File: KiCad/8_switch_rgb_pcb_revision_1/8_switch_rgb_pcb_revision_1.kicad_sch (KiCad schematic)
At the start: 97 parts, among them SW0 SW0, SW1 SW1, SW2 SW2, SW3 SW3, SW4 SW4, SW5 SW5, SW6 SW6, SW7 SW7, U2 74HC165, Y1 16MHz

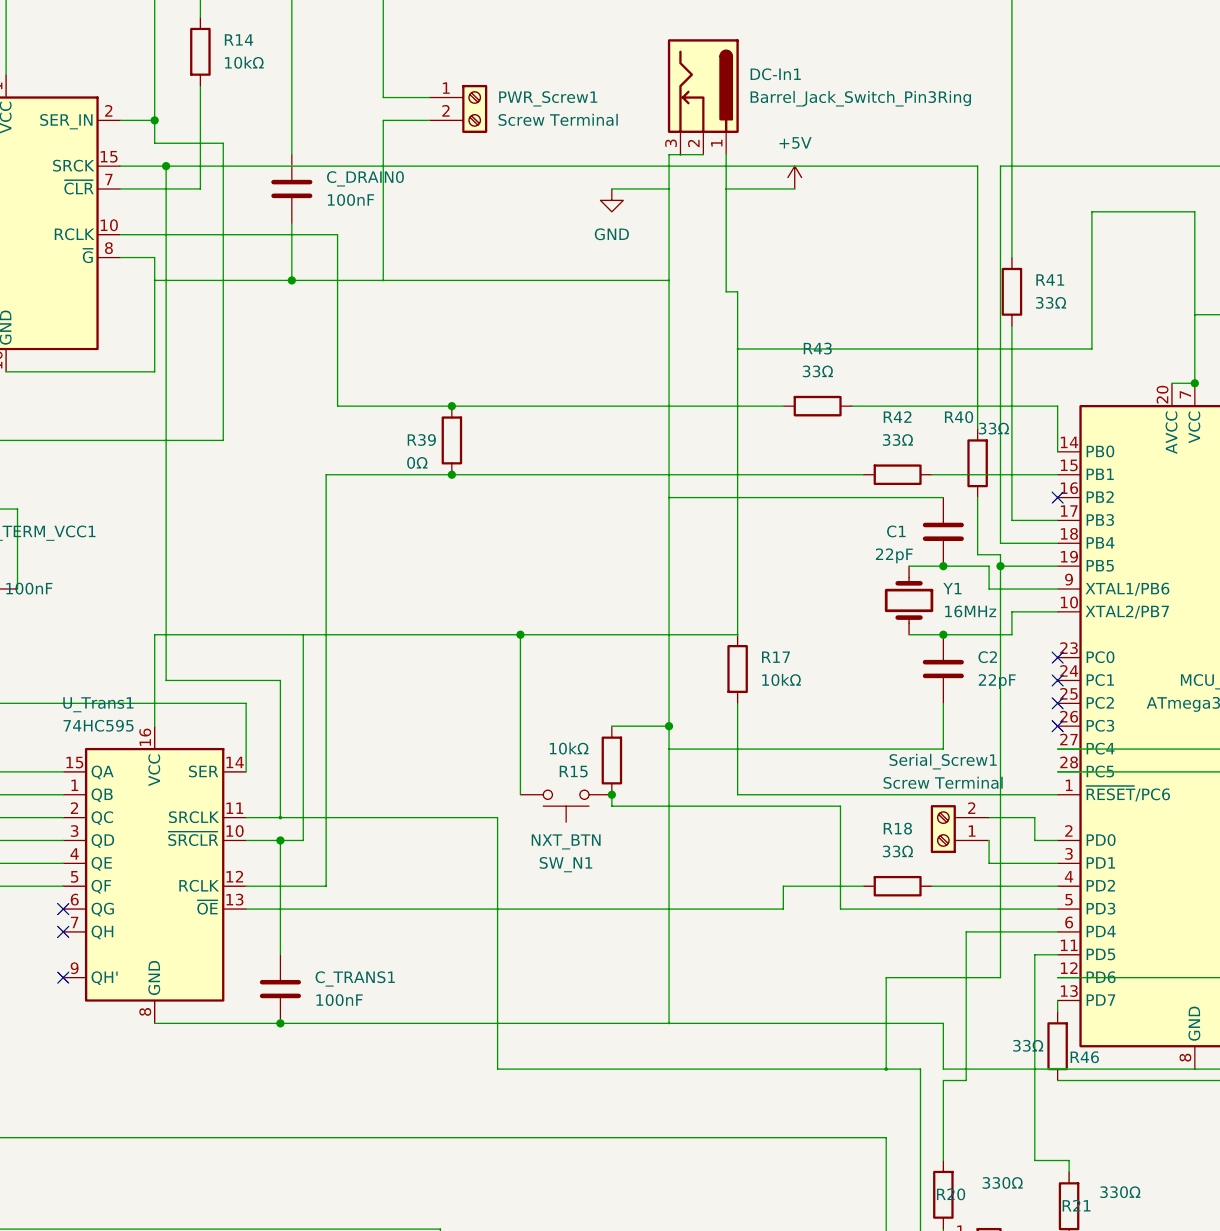
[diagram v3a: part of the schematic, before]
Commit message: Added gerbers, will look at ground plane
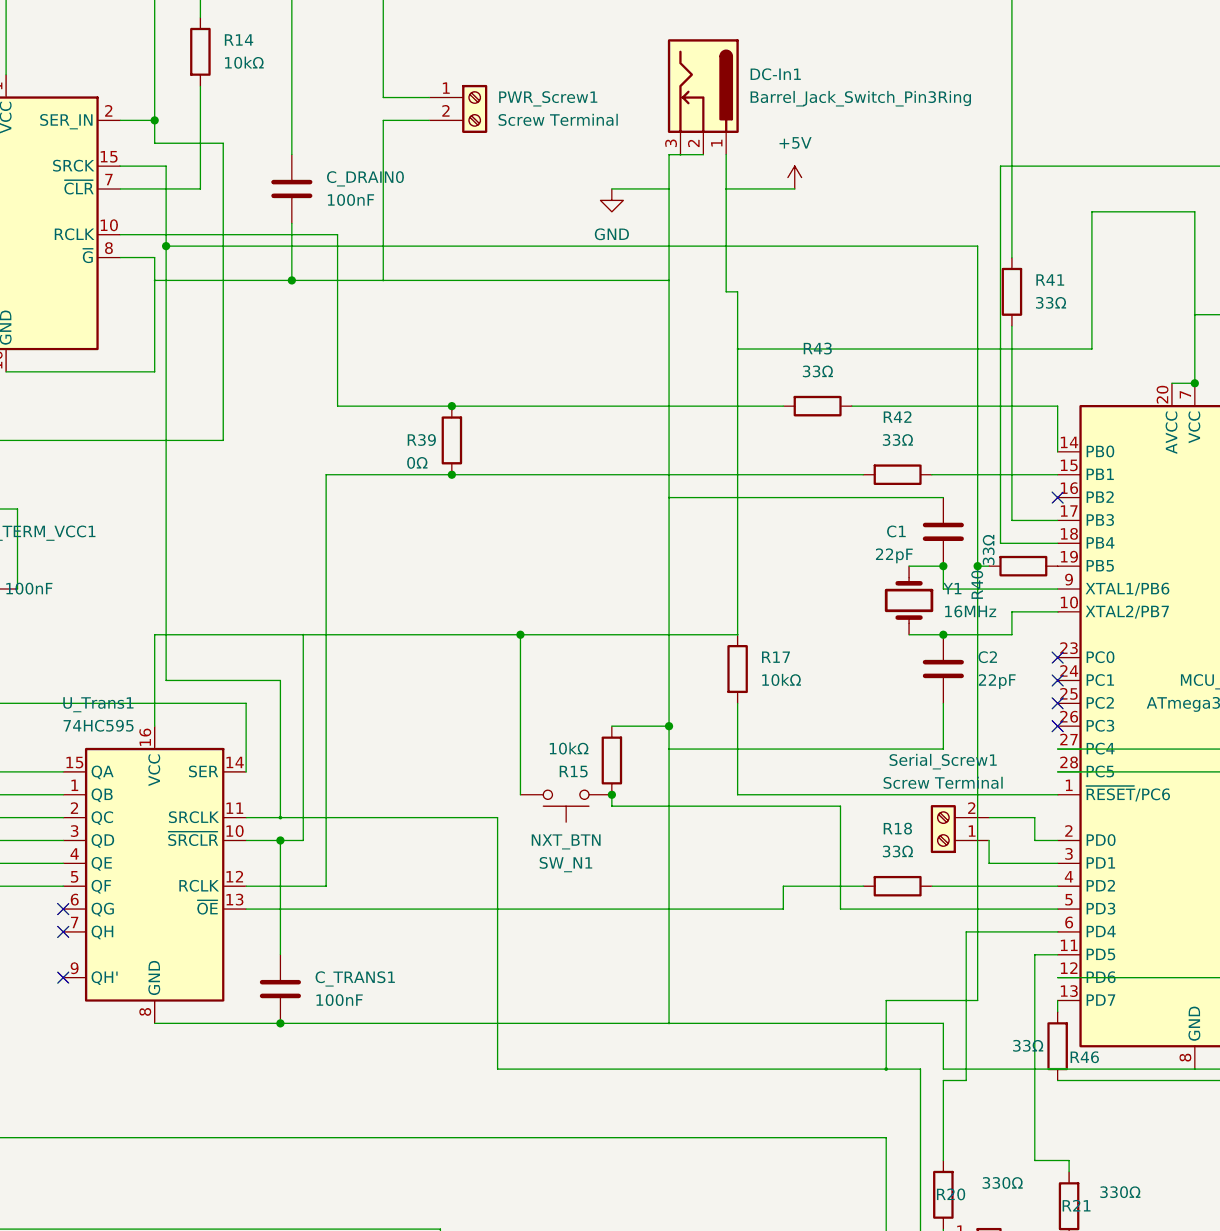
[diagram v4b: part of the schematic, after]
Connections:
- net at R22.1, R40.2, U2.2 (CP)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: no longer MCU_1.19 (PB5), R40.1
- new net: MCU_1.19 (PB5), R40.1
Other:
- moved on the sheet: R40
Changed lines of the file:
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@@
   (junction (at 113.03 83.82) (diameter 0) (color 0 0 0 0)
   )
-  (junction (at 238.76 81.28) (diameter 0) (color 0 0 0 0)
-  )
   (junction (at 177.8 63.5) (diameter 0) (color 0 0 0 0)
   )
@@
   (junction (at 326.39 41.91) (diameter 0) (color 0 0 0 0)
   )
+  (junction (at 146.05 45.72) (diameter 0) (color 0 0 0 0)
+  )
   (junction (at 201.93 39.37) (diameter 0.2) (color 0 0 0 1)
   )
@@
   (junction (at 114.3 180.34) (diameter 0) (color 0 0 0 0)
   )
+  (junction (at 236.22 81.28) (diameter 0) (color 0 0 0 0)
+  )
   (junction (at 304.8 82.55) (diameter 0) (color 0 0 0 0)
   )
@@
   (junction (at 392.43 111.76) (diameter 0.2) (color 255 0 0 1)
   )
-  (junction (at 146.05 36.83) (diameter 0) (color 0 0 0 0)
-  )
   (junction (at 69.85 119.38) (diameter 0) (color 0 0 0 0)
   )
@@
     (stroke (width 0) (type default))
   )
-  (wire (pts (xy 245.11 83.82) (xy 237.49 83.82))
+  (wire (pts (xy 232.41 83.82) (xy 245.11 83.82))
     (stroke (width 0) (type default))
   )
@@
     (stroke (width 0.2) (type default) (color 255 0 0 1))
   )
-  (wire (pts (xy 236.22 36.83) (xy 236.22 66.04))
-    (stroke (width 0.3) (type default) (color 255 255 0 1))
-  )
   (wire (pts (xy 92.71 34.29) (xy 72.39 34.29))
     (stroke (width 0) (type default))
@@
     (stroke (width 0.2) (type default) (color 255 0 0 1))
   )
-  (wire (pts (xy 236.22 73.66) (xy 236.22 80.01))
-    (stroke (width 0.3) (type default) (color 255 255 0 1))
-  )
   (wire (pts (xy 115.57 49.53) (xy 113.03 49.53))
     (stroke (width 0) (type default))
@@
     (stroke (width 0) (type default))
   )
-  (wire (pts (xy 238.76 81.28) (xy 238.76 127))
-    (stroke (width 0.3) (type default) (color 255 255 0 1))
-  )
   (wire (pts (xy 67.31 170.18) (xy 63.5 170.18))
     (stroke (width 0) (type default))
@@
     (stroke (width 0) (type default))
   )
-  (wire (pts (xy 238.76 81.28) (xy 245.11 81.28))
-    (stroke (width 0.3) (type default) (color 255 255 0 1))
-  )
   (wire (pts (xy 60.96 217.17) (xy 60.96 208.28))
     (stroke (width 0) (type default))
@@
     (stroke (width 0) (type default))
   )
+  (wire (pts (xy 146.05 36.83) (xy 146.05 45.72))
+    (stroke (width 0.3) (type default) (color 255 255 0 1))
+  )
   (wire (pts (xy 115.57 34.29) (xy 100.33 34.29))
     (stroke (width 0) (type default))
@@
     (stroke (width 0) (type default))
   )
-  (wire (pts (xy 226.06 137.16) (xy 226.06 127))
+  (wire (pts (xy 226.06 137.16) (xy 226.06 129.54))
     (stroke (width 0.3) (type default) (color 255 255 0 1))
   )
@@
     (stroke (width 0) (type default))
   )
-  (wire (pts (xy 146.05 36.83) (xy 236.22 36.83))
-    (stroke (width 0.3) (type default) (color 255 255 0 1))
-  )
   (wire (pts (xy 360.68 168.91) (xy 360.68 138.43))
     (stroke (width 0) (type default))
@@
     (stroke (width 0.3) (type default) (color 255 255 0 1))
   )
-  (wire (pts (xy 237.49 83.82) (xy 237.49 81.28))
-    (stroke (width 0) (type default))
-  )
   (wire (pts (xy 365.76 167.64) (xy 398.78 167.64))
     (stroke (width 0.2) (type default) (color 0 0 0 1))
@@
     (stroke (width 0) (type default))
   )
-  (wire (pts (xy 226.06 127) (xy 238.76 127))
+  (wire (pts (xy 226.06 129.54) (xy 236.22 129.54))
     (stroke (width 0.3) (type default) (color 255 255 0 1))
   )
@@
     (stroke (width 0.2) (type default) (color 255 0 0 1))
   )
+  (wire (pts (xy 146.05 45.72) (xy 146.05 93.98))
+    (stroke (width 0.3) (type default) (color 255 255 0 1))
+  )
   (wire (pts (xy 72.39 34.29) (xy 72.39 73.66))
     (stroke (width 0) (type default))
@@
     (stroke (width 0) (type default))
   )
+  (wire (pts (xy 146.05 45.72) (xy 236.22 45.72))
+    (stroke (width 0.3) (type default) (color 255 255 0 1))
+  )
   (wire (pts (xy 72.39 132.08) (xy 72.39 193.04))
     (stroke (width 0) (type default))
@@
     (stroke (width 0) (type default))
   )
+  (wire (pts (xy 232.41 83.82) (xy 232.41 81.28))
+    (stroke (width 0) (type default))
+  )
   (wire (pts (xy 115.57 39.37) (xy 114.3 39.37))
     (stroke (width 0) (type default))
@@
     (stroke (width 0) (type default))
   )
+  (wire (pts (xy 236.22 81.28) (xy 237.49 81.28))
+    (stroke (width 0.3) (type default) (color 255 255 0 1))
+  )
   (wire (pts (xy 353.06 109.22) (xy 353.06 179.07))
     (stroke (width 0) (type default))
@@
     (stroke (width 0.2) (type default) (color 0 0 0 1))
   )
-  (wire (pts (xy 237.49 81.28) (xy 232.41 81.28))
-    (stroke (width 0) (type default))
-  )
   (wire (pts (xy 36.83 128.27) (xy 36.83 123.19))
     (stroke (width 0) (type default))
@@
     (stroke (width 0.2) (type default) (color 255 0 0 1))
   )
-  (wire (pts (xy 238.76 80.01) (xy 238.76 81.28))
+  (wire (pts (xy 236.22 81.28) (xy 236.22 129.54))
     (stroke (width 0.3) (type default) (color 255 255 0 1))
   )
@@
     (stroke (width 0) (type default))
   )
-  (wire (pts (xy 146.05 36.83) (xy 146.05 93.98))
-    (stroke (width 0.3) (type default) (color 255 255 0 1))
-  )
   (wire (pts (xy 240.03 54.61) (xy 240.03 76.2))
     (stroke (width 0.4) (type default) (color 0 0 255 1))
@@
     (stroke (width 0) (type default))
   )
-  (wire (pts (xy 236.22 80.01) (xy 238.76 80.01))
-    (stroke (width 0.3) (type default) (color 255 255 0 1))
-  )
   (wire (pts (xy 30.48 69.85) (xy 36.83 69.85))
     (stroke (width 0) (type default))
@@
     (stroke (width 0) (type default))
   )
+  (wire (pts (xy 236.22 45.72) (xy 236.22 81.28))
+    (stroke (width 0.3) (type default) (color 255 255 0 1))
+  )
   (wire (pts (xy 354.33 181.61) (xy 349.25 181.61))
     (stroke (width 0) (type default))
@@
     )
   )
-  (symbol (lib_id "Device:R") (at 236.22 69.85 180) (unit 1)
+  (symbol (lib_id "Device:R") (at 241.3 81.28 270) (unit 1)
     (in_bom yes) (on_board yes) (dnp no)
-    (property "Reference" "R40" (at 232.41 64.77 0)
+    (property "Reference" "R40" (at 236.22 85.09 0)
       (effects (font (size 1.27 1.27)) (justify right))
     )
-    (property "Value" "33Ω" (at 236.22 66.04 0)
+    (property "Value" "33Ω" (at 237.49 81.28 0)
       (effects (font (size 1.27 1.27)) (justify right))
     )
-    (property "Footprint" "Resistor_THT:R_Axial_DIN0204_L3.6mm_D1.6mm_P5.08mm_Horizontal" (at 237.998 69.85 90)
+    (property "Footprint" "Resistor_THT:R_Axial_DIN0204_L3.6mm_D1.6mm_P5.08mm_Horizontal" (at 241.3 79.502 90)
       (effects (font (size 1.27 1.27)) hide)
     )
-    (property "Datasheet" "~" (at 236.22 69.85 0)
+    (property "Datasheet" "~" (at 241.3 81.28 0)
       (effects (font (size 1.27 1.27)) hide)
     )
